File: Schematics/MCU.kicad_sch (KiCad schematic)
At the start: 34 parts, among them J1 Microsemi_FlashPro-JTAG-10, Q3 BC817, SW1 SAMZO G4R0015010, SW2 SAMZO G4R0015010, U1 STM32F405RGT6, Y1 8mhz

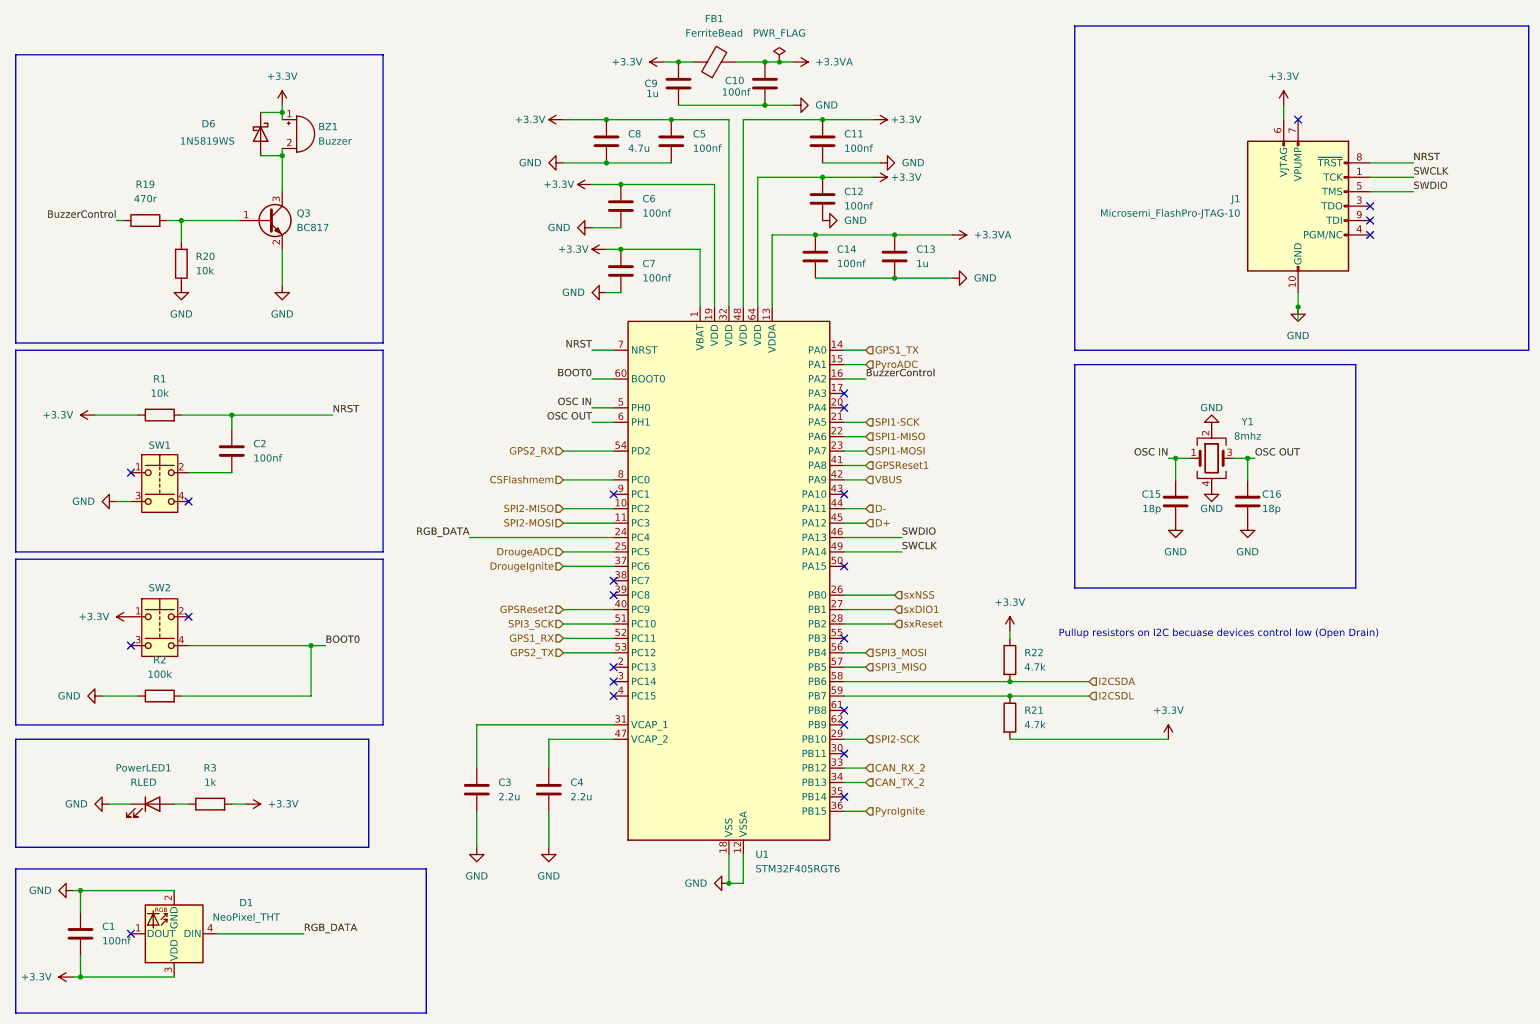
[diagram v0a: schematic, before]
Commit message: added aux pyro added reverse polarity protection re routed just need to clean up and check pin assignments
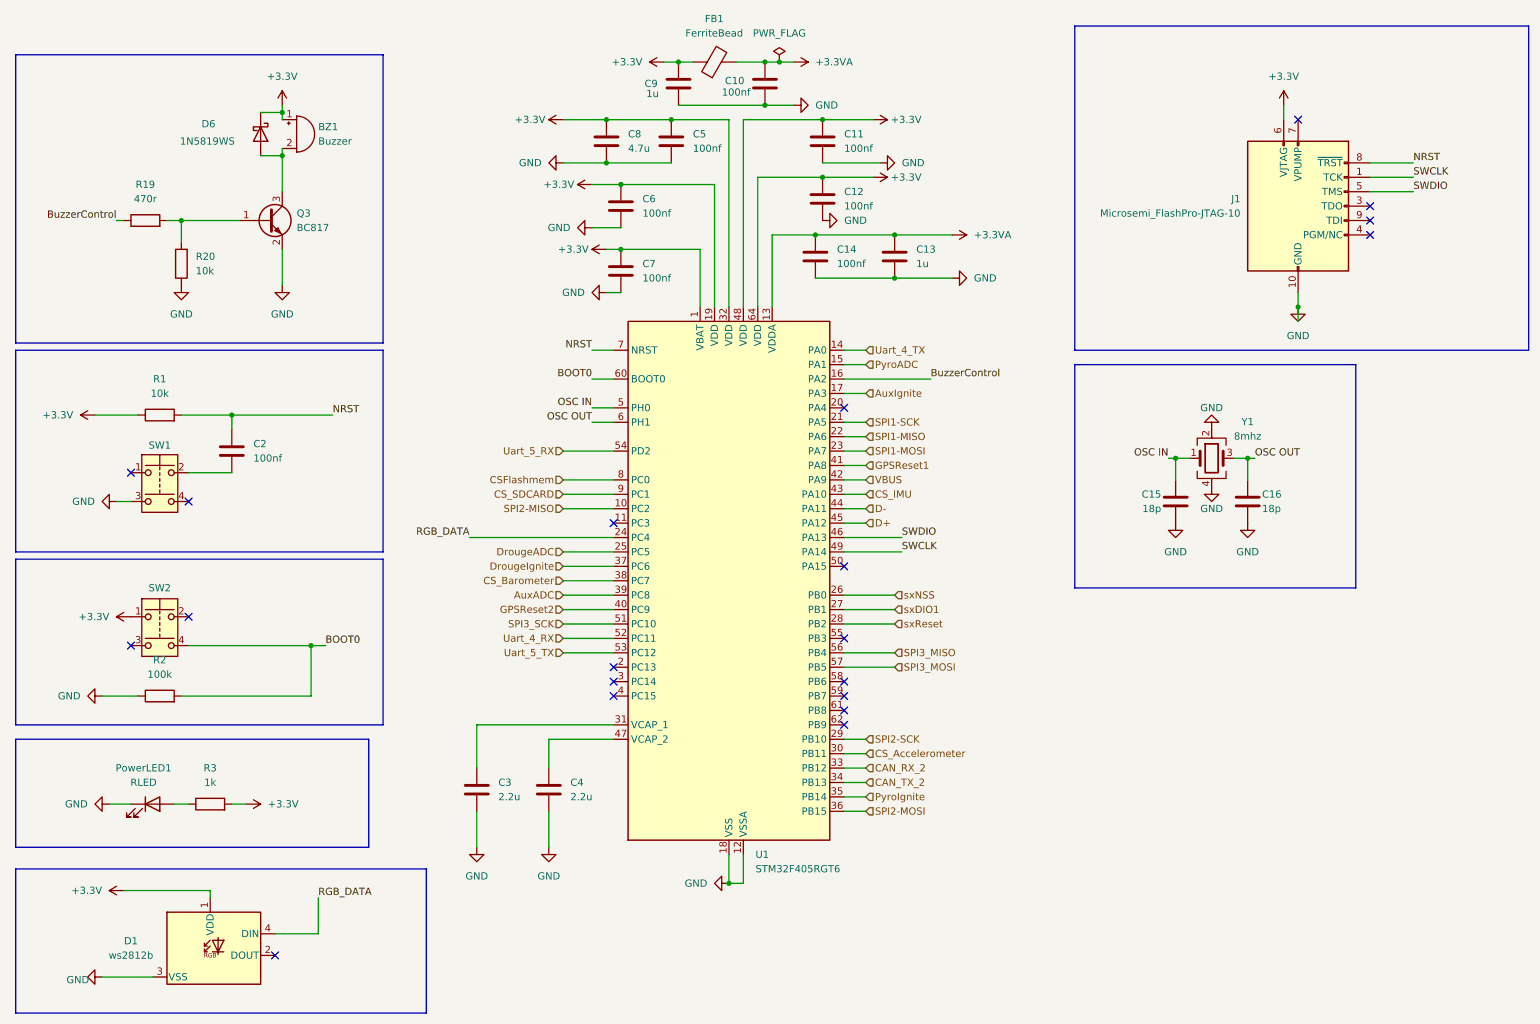
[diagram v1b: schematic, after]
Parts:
- removed C1: 100nf, Capacitor_SMD:C_0805_2012Metric_Pad1.18x1.45mm_HandSolder, symbol Device:C
- removed R21, R22: 4.7k, Resistor_SMD:R_0805_2012Metric_Pad1.20x1.40mm_HandSolder, symbol Device:R
- D1: value NeoPixel_THT -> ws2812b; footprint LED_SMD:LED_Kingbright_AAA3528ESGCT -> LED_SMD:LED_WS2812B_PLCC4_5.0x5.0mm_P3.2mm; LCSC C2827321 -> C114586
- J1: LCSC C585350 -> C588426
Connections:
- net +3.3V: now also D1.1 (VDD); no longer D1.3 (VDD)
- net GND: now also D1.3 (VSS); no longer D1.2 (GND)
- net PyroIgnite: now also U1.35 (PB14); no longer U1.36 (PB15)
- net SPI2-MOSI: now also U1.36 (PB15); no longer U1.11 (PC3)
- net SPI3_MISO: now also U1.56 (PB4); no longer U1.57 (PB5)
- net SPI3_MOSI: now also U1.57 (PB5); no longer U1.56 (PB4)
- net AuxIgnite: now reaches U1.17 (PA3)
- net CS_Accelerometer: now reaches U1.30 (PB11)
- net CS_Barometer: now reaches U1.38 (PC7)
- net AuxADC: now reaches U1.39 (PC8)
- net CS_IMU: now reaches U1.43 (PA10)
- net CS_SDCARD: now reaches U1.9 (PC1)
- net GPS1_RX renamed Uart_4_RX
- net GPS1_TX renamed Uart_4_TX
- net GPS2_RX renamed Uart_5_RX
- net GPS2_TX renamed Uart_5_TX
- net I2CSDA: no longer names the net of U1.58 (PB6)
- net I2CSDL: no longer names the net of U1.59 (PB7)
- no-connect marks 24 -> 20
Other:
- note removed: "Pullup resistors on I2C becuase devices control low (Open Drain)"
- moved on the sheet: D1

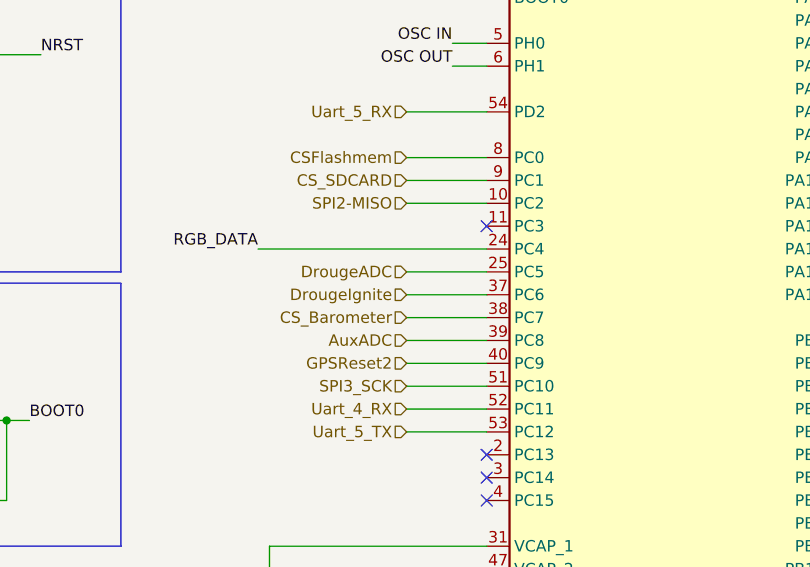
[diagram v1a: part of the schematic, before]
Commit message: layout completed added testpoints and verified mosfet ect
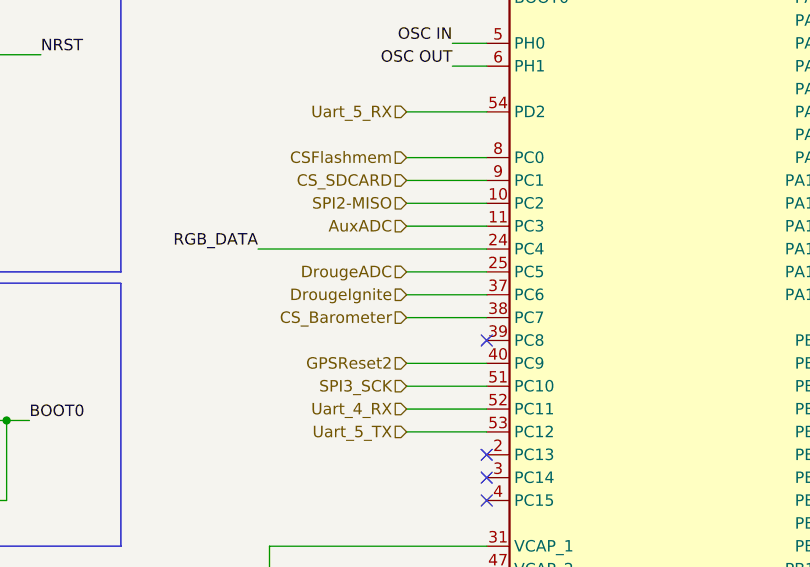
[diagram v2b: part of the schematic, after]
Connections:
- net AuxADC: now also U1.11 (PC3); no longer U1.39 (PC8)
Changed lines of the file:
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@@
-	)
-	(no_connect
-		(at 120.65 107.95)
 	)
 	(no_connect
@@
 		(at 60.96 184.15)
 	)
+	(no_connect
+		(at 120.65 120.65)
+	)
 	(wire
 		(pts
@@
 	(wire
 		(pts
-			(xy 111.76 120.65) (xy 120.65 120.65)
+			(xy 111.76 107.95) (xy 120.65 107.95)
 		)
 		(stroke
@@
 	(hierarchical_label "AuxADC"
 		(shape input)
-		(at 111.76 120.65 180)
-		(effects
-			(font
+		(at 111.76 107.95 180)
+		(effects
+			(font
